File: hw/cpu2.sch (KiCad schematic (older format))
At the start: 0 parts

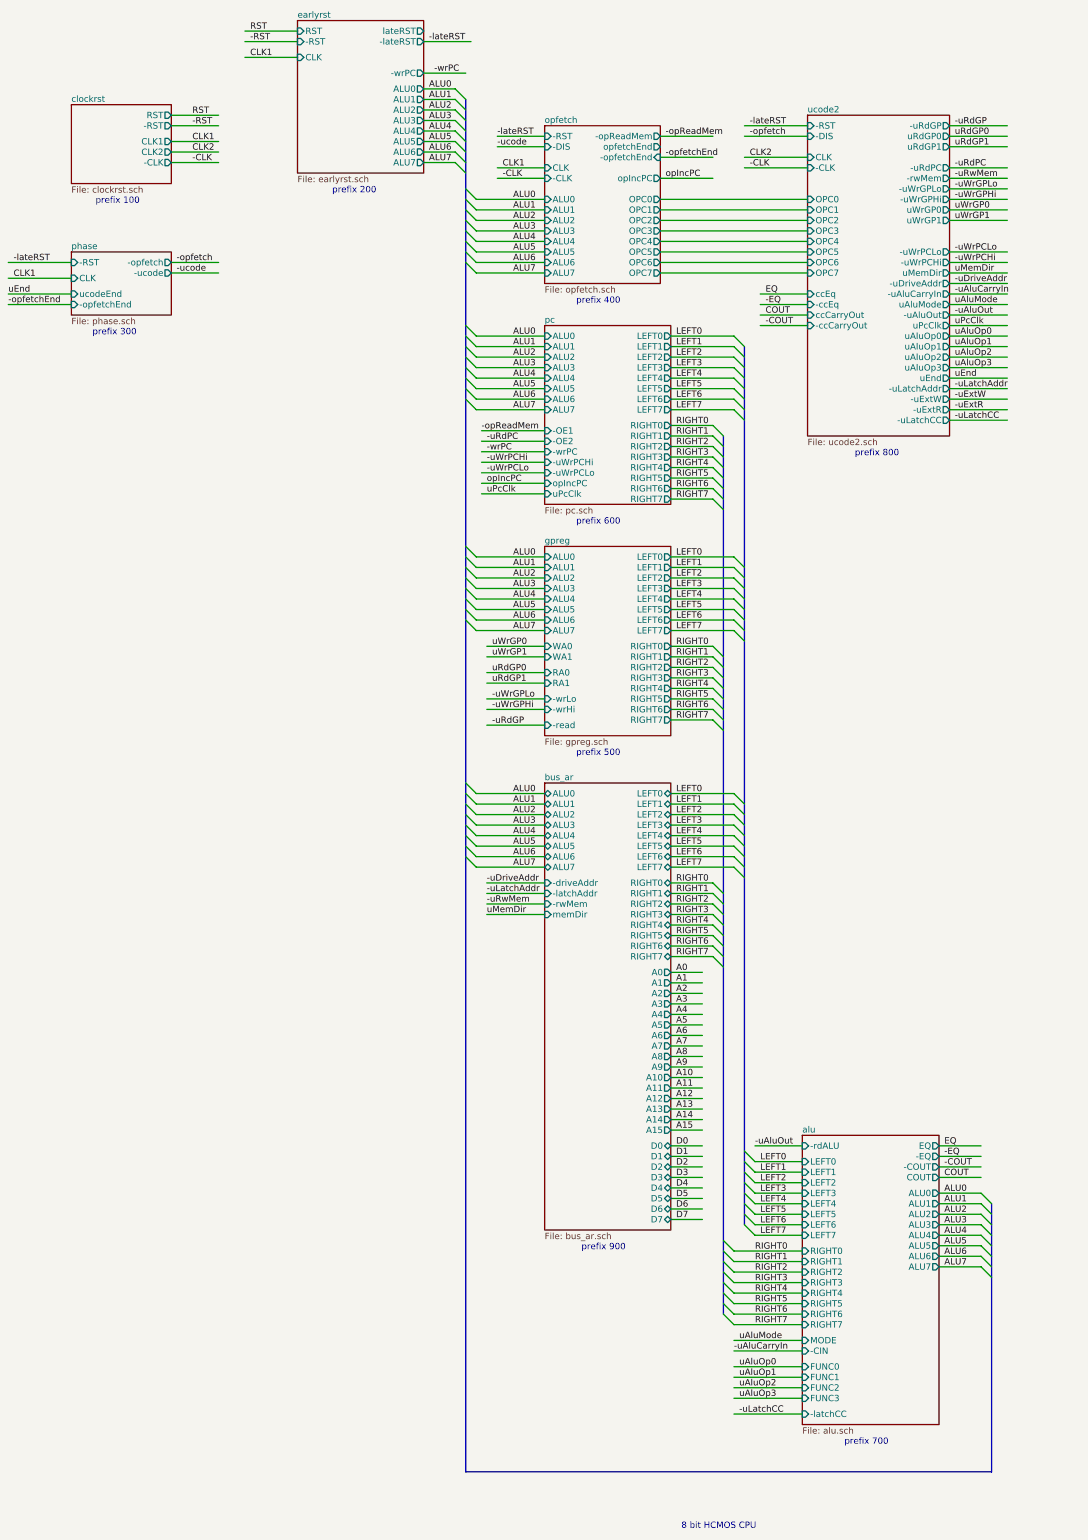
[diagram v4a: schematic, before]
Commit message: add missing signals to/from ucode2 module
Also, use a custom page size for the top-level
schematic.
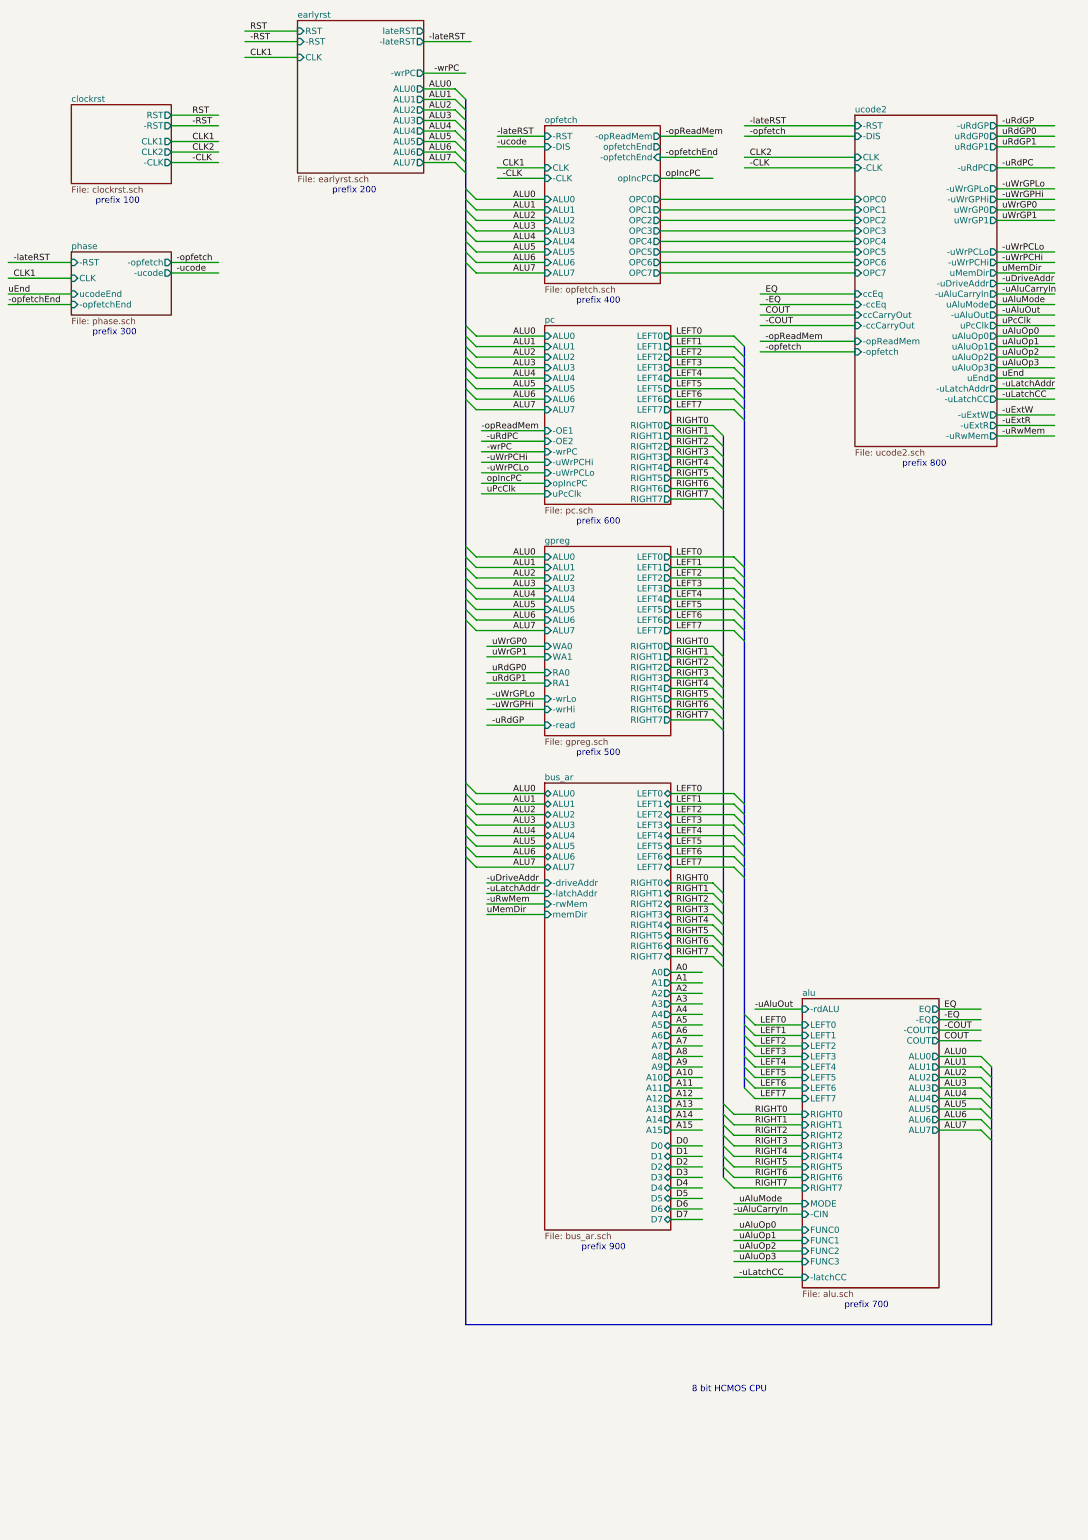
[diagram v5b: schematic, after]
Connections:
- wire segments 231 -> 233

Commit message: replace '193 with '393 in opfetch module
The '393 has two fewer pins, better use of breadboard space.
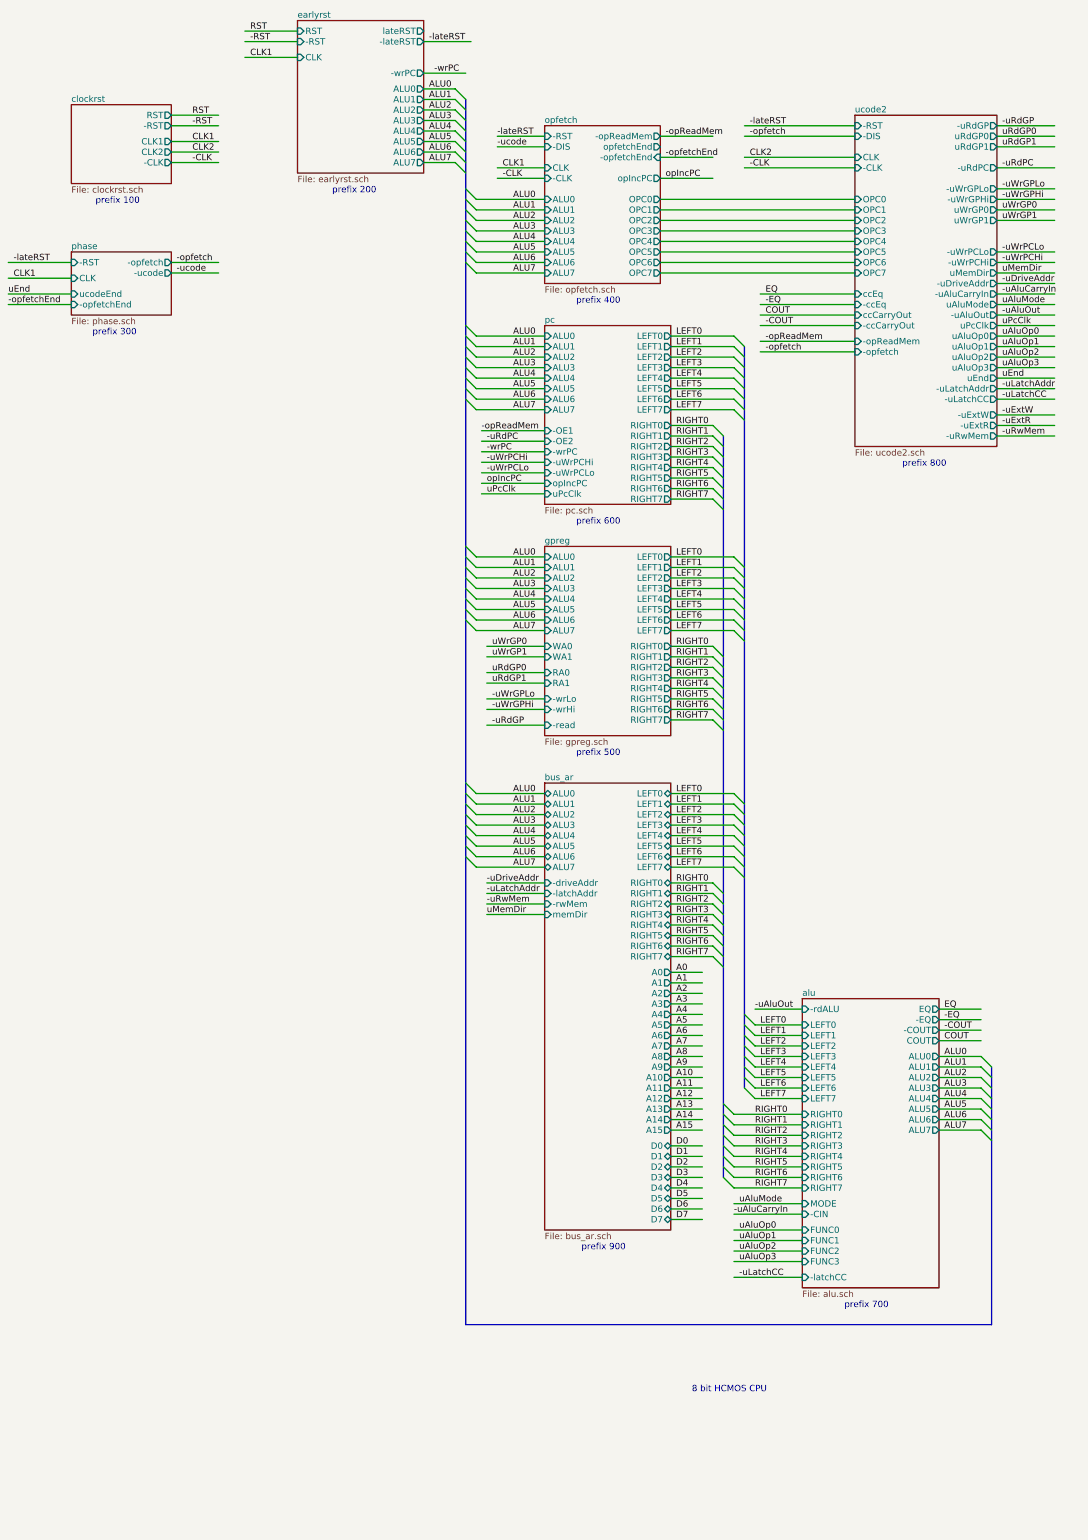
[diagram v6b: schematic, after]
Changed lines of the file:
@@
 	4700 2050 5000 2050
 Wire Bus Line
-	5100 1450 5100 1550
-Wire Bus Line
-	5100 1550 5100 1650
-Wire Bus Line
-	5100 1650 5100 1750
-Wire Bus Line
-	5100 1750 5100 1850
-Wire Bus Line
-	5100 1850 5100 1950
-Wire Bus Line
-	5100 1950 5100 2050
-Wire Bus Line
-	5100 2050 5100 2150
-Wire Bus Line
-	5100 2150 5100 2300
-Wire Bus Line
-	5100 2300 5100 2400
-Wire Bus Line
-	5100 2400 5100 2500
-Wire Bus Line
-	5100 2500 5100 2600
-Wire Bus Line
-	5100 2600 5100 2700
-Wire Bus Line
-	5100 2700 5100 2800
-Wire Bus Line
-	5100 2800 5100 2900
-Wire Bus Line
-	5100 2900 5100 3000
-Wire Bus Line
-	5100 3000 5100 3600
-Wire Bus Line
-	5100 3600 5100 3700
-Wire Bus Line
-	5100 3700 5100 3800
-Wire Bus Line
-	5100 3800 5100 3900
-Wire Bus Line
-	5100 3900 5100 4000
-Wire Bus Line
-	5100 4000 5100 4100
-Wire Bus Line
-	5100 4100 5100 4200
-Wire Bus Line
-	5100 4200 5100 4300
-Wire Bus Line
-	5100 4300 5100 5700
-Wire Bus Line
-	5100 5700 5100 5800
-Wire Bus Line
-	5100 5800 5100 5900
-Wire Bus Line
-	5100 5900 5100 6000
-Wire Bus Line
-	5100 6000 5100 6100
-Wire Bus Line
-	5100 6100 5100 6200
-Wire Bus Line
-	5100 6200 5100 6300
-Wire Bus Line
-	5100 6300 5100 6400
-Wire Bus Line
-	5100 6400 5100 7950
-Wire Bus Line
-	5100 7950 5100 8050
-Wire Bus Line
-	5100 8050 5100 8150
-Wire Bus Line
-	5100 8150 5100 8250
-Wire Bus Line
-	5100 8250 5100 8350
-Wire Bus Line
-	5100 8350 5100 8450
-Wire Bus Line
-	5100 8450 5100 8550
-Wire Bus Line
-	5100 8550 5100 8650
-Wire Bus Line
-	5100 8650 5100 13100
+	5100 1450 5100 13100
 Wire Wire Line
 	5850 2400 5200 2400
@@
 	7050 4400 7650 4400
 Wire Bus Line
-	7750 3800 7750 3900
-Wire Bus Line
-	7750 3900 7750 4000
-Wire Bus Line
-	7750 4000 7750 4100
-Wire Bus Line
-	7750 4100 7750 4200
-Wire Bus Line
-	7750 4200 7750 4300
-Wire Bus Line
-	7750 4300 7750 4400
-Wire Bus Line
-	7750 4400 7750 4500
-Wire Bus Line
-	7750 4500 7750 5900
-Wire Bus Line
-	7750 5900 7750 6000
-Wire Bus Line
-	7750 6000 7750 6100
-Wire Bus Line
-	7750 6100 7750 6200
-Wire Bus Line
-	7750 6200 7750 6300
-Wire Bus Line
-	7750 6300 7750 6400
-Wire Bus Line
-	7750 6400 7750 6500
-Wire Bus Line
-	7750 6500 7750 6600
-Wire Bus Line
-	7750 6600 7750 8150
-Wire Bus Line
-	7750 8150 7750 8250
-Wire Bus Line
-	7750 8250 7750 8350
-Wire Bus Line
-	7750 8350 7750 8450
-Wire Bus Line
-	7750 8450 7750 8550
-Wire Bus Line
-	7750 8550 7750 8650
-Wire Bus Line
-	7750 8650 7750 8750
-Wire Bus Line
-	7750 8750 7750 8850
-Wire Bus Line
-	7750 8850 7750 10150
-Wire Bus Line
-	7750 10150 7750 10250
-Wire Bus Line
-	7750 10250 7750 10350
-Wire Bus Line
-	7750 10350 7750 10450
-Wire Bus Line
-	7750 10450 7750 10550
-Wire Bus Line
-	7750 10550 7750 10650
-Wire Bus Line
-	7750 10650 7750 10750
-Wire Bus Line
-	7750 10750 7750 10850
+	7750 3800 7750 10850
 Wire Wire Line
 	8300 10250 7850 10250
@@
 	7050 5250 7450 5250
 Wire Bus Line
-	7550 4650 7550 4750
-Wire Bus Line
-	7550 4750 7550 4850
-Wire Bus Line
-	7550 4850 7550 4950
-Wire Bus Line
-	7550 4950 7550 5050
-Wire Bus Line
-	7550 5050 7550 5150
-Wire Bus Line
-	7550 5150 7550 5250
-Wire Bus Line
-	7550 5250 7550 5350
-Wire Bus Line
-	7550 5350 7550 6750
-Wire Bus Line
-	7550 6750 7550 6850
-Wire Bus Line
-	7550 6850 7550 6950
-Wire Bus Line
-	7550 6950 7550 7050
-Wire Bus Line
-	7550 7050 7550 7150
-Wire Bus Line
-	7550 7150 7550 7250
-Wire Bus Line
-	7550 7250 7550 7350
-Wire Bus Line
-	7550 7350 7550 7450
-Wire Bus Line
-	7550 7450 7550 9000
-Wire Bus Line
-	7550 9000 7550 9100
-Wire Bus Line
-	7550 9100 7550 9200
-Wire Bus Line
-	7550 9200 7550 9300
-Wire Bus Line
-	7550 9300 7550 9400
-Wire Bus Line
-	7550 9400 7550 9500
-Wire Bus Line
-	7550 9500 7550 9600
-Wire Bus Line
-	7550 9600 7550 9700
-Wire Bus Line
-	7550 9700 7550 11000
-Wire Bus Line
-	7550 11000 7550 11100
-Wire Bus Line
-	7550 11100 7550 11200
-Wire Bus Line
-	7550 11200 7550 11300
-Wire Bus Line
-	7550 11300 7550 11400
-Wire Bus Line
-	7550 11400 7550 11500
-Wire Bus Line
-	7550 11500 7550 11600
-Wire Bus Line
-	7550 11600 7550 11700
+	7550 4650 7550 11700
 Wire Wire Line
 	8300 11100 7650 11100
@@
 	10100 13100 5100 13100
 Wire Bus Line
-	10100 10650 10100 10750
-Wire Bus Line
-	10100 10750 10100 10850
-Wire Bus Line
-	10100 10850 10100 10950
-Wire Bus Line
-	10100 10950 10100 11050
-Wire Bus Line
-	10100 11050 10100 11150
-Wire Bus Line
-	10100 11150 10100 11250
-Wire Bus Line
-	10100 11250 10100 11350
-Wire Bus Line
-	10100 11350 10100 13100
+	10100 10650 10100 13100
 Wire Wire Line
 	9600 10550 10000 10550
